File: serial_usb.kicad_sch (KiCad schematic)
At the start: 24 parts, among them J2 3V3 Serial, J3 USB_C_USB2.0_16P, U17 ST16C550, U18 CP2102N, Y2 3.6864MHz

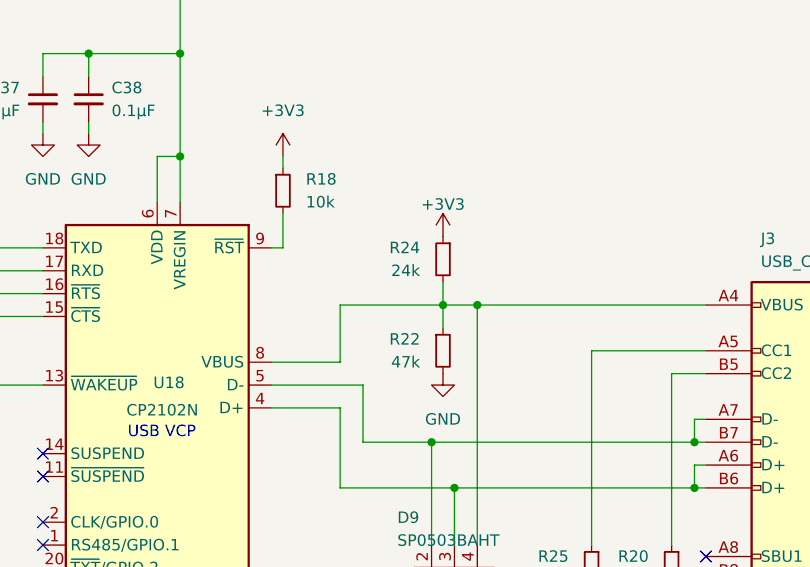
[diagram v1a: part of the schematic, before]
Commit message: fix VUSB bug
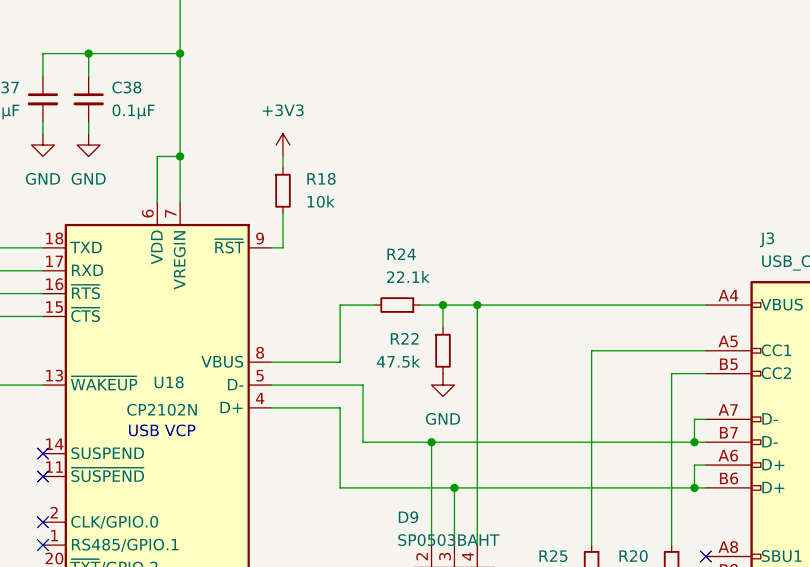
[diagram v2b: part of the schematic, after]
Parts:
- R22: value 47k -> 47.5k
- R24: value 24k -> 22.1k
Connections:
- net +3V3: no longer R24.1
- net at D9.4 (K), J3.A4 (VBUS), J3.A9 (VBUS)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: now also R24.1; no longer R24.2, U18.8 (VBUS)
- new net: R24.2, U18.8 (VBUS)
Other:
- moved on the sheet: R24
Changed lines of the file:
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@@
 	(wire
 		(pts
-			(xy 264.16 148.59) (xy 264.16 151.13)
-		)
-		(stroke
-			(width 0)
-			(type default)
-		)
-	)
-	(wire
-		(pts
 			(xy 210.82 147.32) (xy 219.71 147.32)
 		)
@@
 	(wire
 		(pts
-			(xy 264.16 151.13) (xy 252.73 151.13)
+			(xy 264.16 151.13) (xy 261.62 151.13)
 		)
 		(stroke
@@
 	(wire
 		(pts
+			(xy 256.54 151.13) (xy 252.73 151.13)
+		)
+		(stroke
+			(width 0)
+			(type default)
+		)
+	)
+	(wire
+		(pts
 			(xy 167.64 123.19) (xy 165.1 123.19)
 		)
@@
 			)
 		)
-		(property "Value" "47k"
+		(property "Value" "47.5k"
 			(at 261.62 157.4799 0)
 			(effects
@@
 	(symbol
 		(lib_id "Device:R_Small")
-		(at 264.16 146.05 0)
-		(mirror y)
+		(at 259.08 151.13 270)
+		(mirror x)
 		(unit 1)
 		(exclude_from_sim no)
@@
 		(dnp no)
 		(property "Reference" "R24"
-			(at 261.62 144.7799 0)
+			(at 257.81 145.542 90)
 			(effects
 				(font
@@
 			)
 		)
-		(property "Value" "24k"
-			(at 261.62 147.3199 0)
+		(property "Value" "22.1k"
+			(at 257.81 148.082 90)
 			(effects
 				(font
@@
 		)
 		(property "Footprint" "Resistor_SMD:R_0402_1005Metric"
-			(at 264.16 146.05 0)
+			(at 259.08 151.13 0)
 			(effects
 				(font
@@
 		)
 		(property "Datasheet" "~"
-			(at 264.16 146.05 0)
+			(at 259.08 151.13 0)
 			(effects
 				(font
@@
 		)
 		(property "Description" "Resistor, small symbol"
-			(at 264.16 146.05 0)
+			(at 259.08 151.13 0)
 			(effects
 				(font
@@
 					(unit 1)
 				)
-			)
-		)
-	)
-	(symbol
-		(lib_id "power:+3V3")
-		(at 264.16 143.51 0)
-		(unit 1)
-		(exclude_from_sim no)
-		(in_bom yes)
-		(on_board yes)
-		(dnp no)
-		(property "Reference" "#PWR068"
-			(at 264.16 147.32 0)
-			(effects
-				(font
-					(size 1.27 1.27)
-				)
-				(hide yes)
-			)
-		)
-		(property "Value" "+3V3"
-			(at 264.16 139.954 0)
-			(effects
-				(font
-					(size 1.27 1.27)
-				)
-			)
-		)
-		(property "Footprint" ""
-			(at 264.16 143.51 0)
-			(effects
-				(font
-					(size 1.27 1.27)
-				)
-				(hide yes)
-			)
-		)
-		(property "Datasheet" ""
-			(at 264.16 143.51 0)
-			(effects
-				(font
-					(size 1.27 1.27)
-				)
-				(hide yes)
-			)
-		)
-		(property "Description" "Power symbol creates a global label with name \"+3V3\""
-			(at 264.16 143.51 0)
-			(effects
-				(font
-					(size 1.27 1.27)
-				)
-				(hide yes)
-			)
-		)
-		(pin "1"
-		)
-		(instances
-			(project "ns32k"
-				(path "/54787df0-1b8c-465f-acae-f55ec7f02da3/88416a49-920c-402a-9500-7be871f57ef4"
-					(reference "#PWR068")
-					(unit 1)
-				)

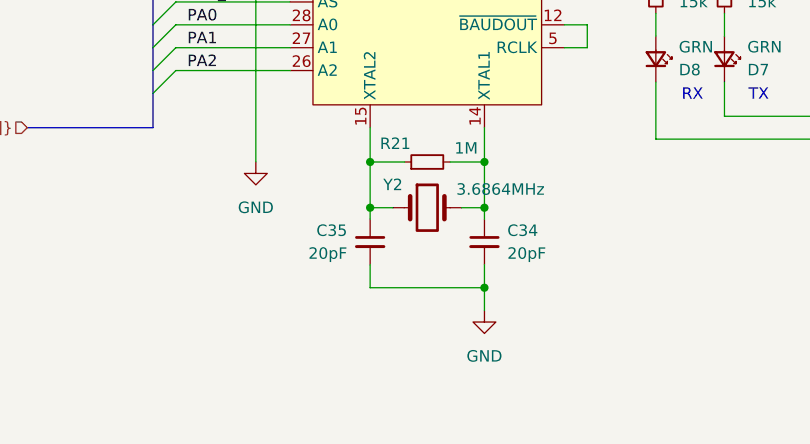
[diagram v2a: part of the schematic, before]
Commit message: route ethernet, reroute USB
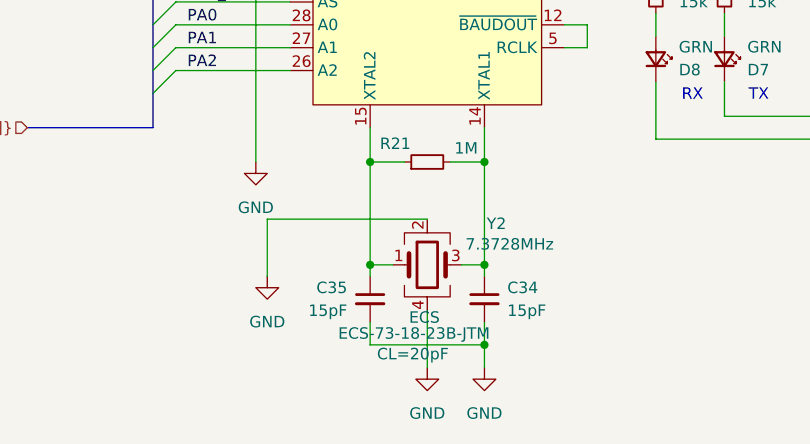
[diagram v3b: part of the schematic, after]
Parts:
- C34, C35: value 20pF -> 15pF
- Y2: value 3.6864MHz -> 7.3728MHz; footprint CSM-7XDU:CSM-7XDU -> Crystal:Crystal_SMD_0603-4Pin_6.0x3.5mm; symbol Device:Crystal -> Device:Crystal_GND24; Mfg (none) -> ECS; Params (none) -> CL=20pF; Part (none) -> ECS-73-18-23B-JTM
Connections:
- net GND: now also Y2.2, Y2.4
- net at C34.1, R21.2, U17.14 (XTAL1): now also Y2.3; no longer Y2.2
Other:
- moved on the sheet: C34, C35
